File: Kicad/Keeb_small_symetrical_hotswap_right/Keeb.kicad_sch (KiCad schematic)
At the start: 32 parts, among them J2 B2B-XH-A_LF__SN_, J3 MJ-4PP-9_MJ-4PP-9, SW1 CherryMX, SW10 CherryMX, SW11 CherryMX, SW13 CherryMX, SW14 CherryMX, SW15 CherryMX, SW16 CherryMX, SW17 CherryMX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

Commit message: Initial commit
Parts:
- removed SW2: CherryMX, ScottoKeebs_Hotswap:Hotswap_MX_Plated_1.00u, symbol Keeb-rescue:CherryMX-CherryMX
- removed U1: Pico, MCU_RaspberryPi_and_Boards:RPi_Pico_SMD_TH_NO_BACK_HOLES, symbol Keeb-rescue:Pico-MCU_RaspberryPi_and_Boards
- added U3: nice_nano, Nice_nano:nice_nano, symbol nice_nano:nice_nano
- J3: footprint MJ-4PP-9:MJ-4PP-9_no_silk -> MJ-4PP-9:MJ-4PP-9
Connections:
- net 0 is gone; now on net 19: SW20.2
- net 26 is gone; now on net GND: SW3.2
- net 27 is gone; now on net GND: SW4.2
- net 28 is gone; now on net 1: SW5.1
- net 1: now also U3.1 (TX0/P0.06); no longer SW1.1
- net 10: now also J3.3 (C), J3.4 (D), U3.12 (P1.06); no longer SW14.2
- net 11: now also U2.DT, U3.31 (P1.01); no longer SW15.2
- net 12: now also U2.CLK, U3.32 (P1.02); no longer SW17.2
- net 13: now also U3.33 (P1.07)
- net 14: now also SW14.2, U3.13 (NFC1/P0.09); no longer J3.3 (C)
- net 15: now also SW15.2, U3.14 (NFC2/P0.10); no longer J3.1 (A)
- net 16: now also SW17.2, U3.15 (P1.11); no longer SW11.1
- net 17: now also SW18.2, U3.16 (P1.13); no longer SW10.1
- net 18: now also SW19.2, U3.17 (P1.15); no longer SW9.1
- net 19: now also U3.18 (AIN0/P0.02); no longer SW6.1
- net 2: now also SW3.1, U3.2 (RX1/P0.08); no longer U2.SW
- net 20: now also SW16.1, U3.19 (AIN5/P0.29); no longer SW7.1
- net 21: now also SW1.2, U3.20 (AIN7/P0.31); no longer SW8.1
- net 3: now also SW4.1, U3.5 (P0.17); no longer SW19.2
- net 3v3: now also J3.1 (A), U3.21 (VCC), U3.24 (BATIN/P0.04); no longer J3.4 (D)
- net 4: now also SW8.1, U3.6 (P0.20); no longer SW16.1
- net 5: now also SW7.1, U3.7 (P0.22); no longer SW18.2
- net 6: now also SW6.1, U3.8 (P0.24)
- net 7: now also SW11.1, U3.9 (P1.00)
- net 8: now also SW10.1, U3.10 (P0.11); no longer U2.CLK
- net 9: now also SW9.1, U3.11 (P1.04); no longer U2.DT
- net GND: now also SW1.1, U3.23 (GND), U3.3 (GND), U3.4 (GND); no longer SW1.2, SW3.1, SW4.1
- new net RST: U3.22 (RST)

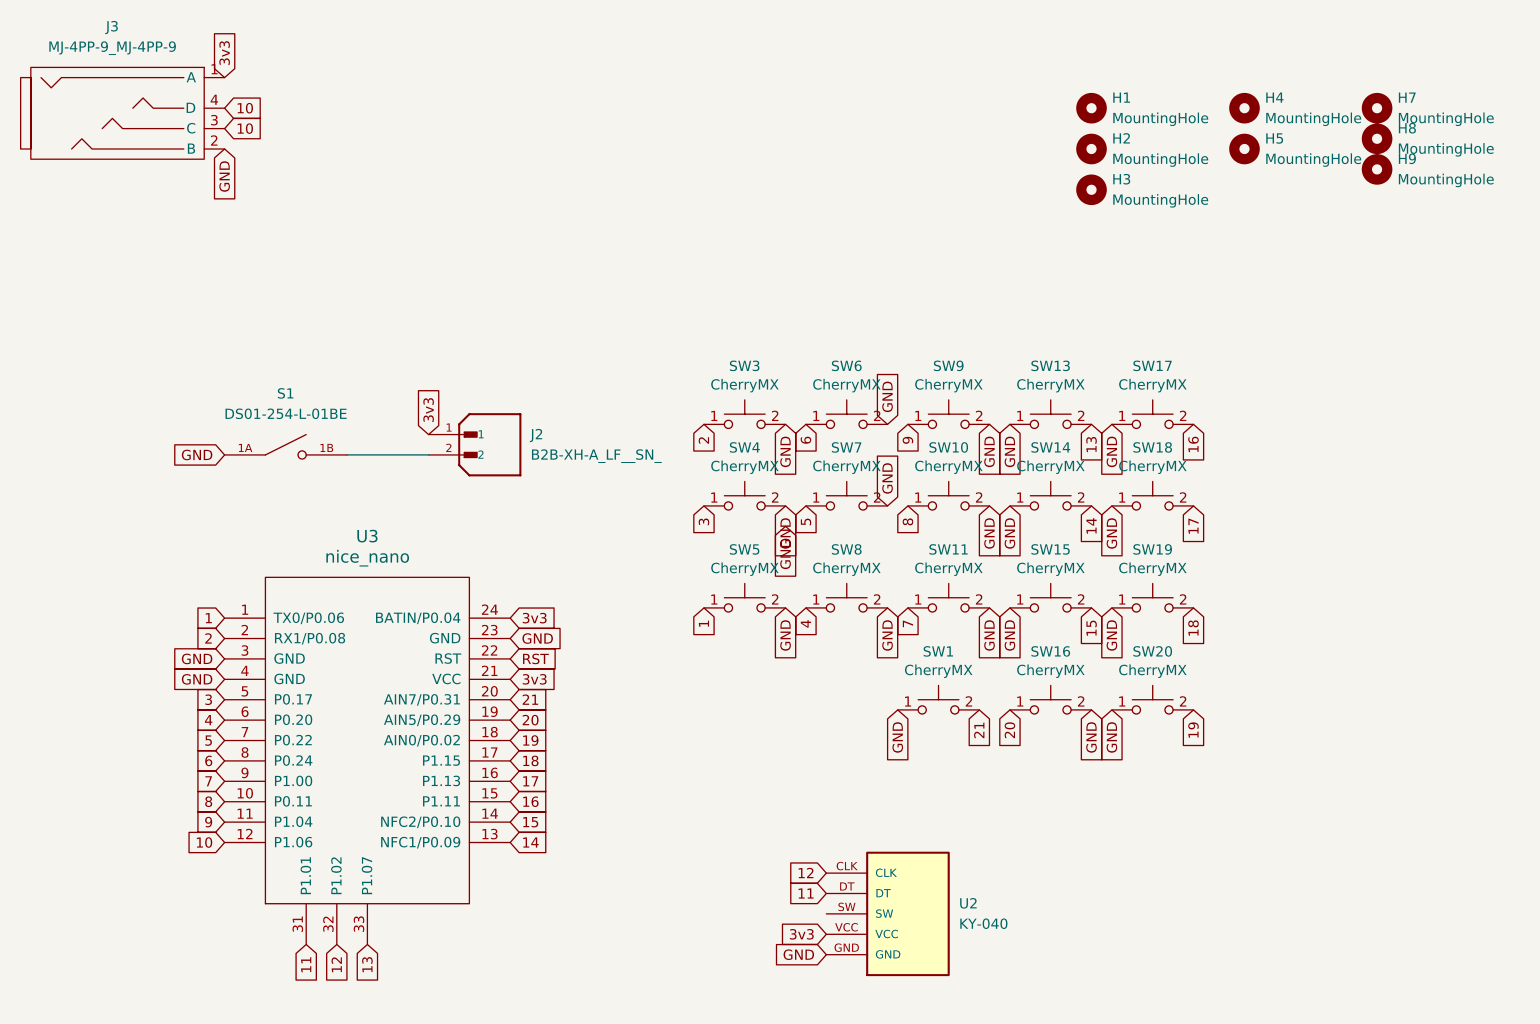
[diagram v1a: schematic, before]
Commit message: current version, all problems fixed, software compiled for CP 9.0
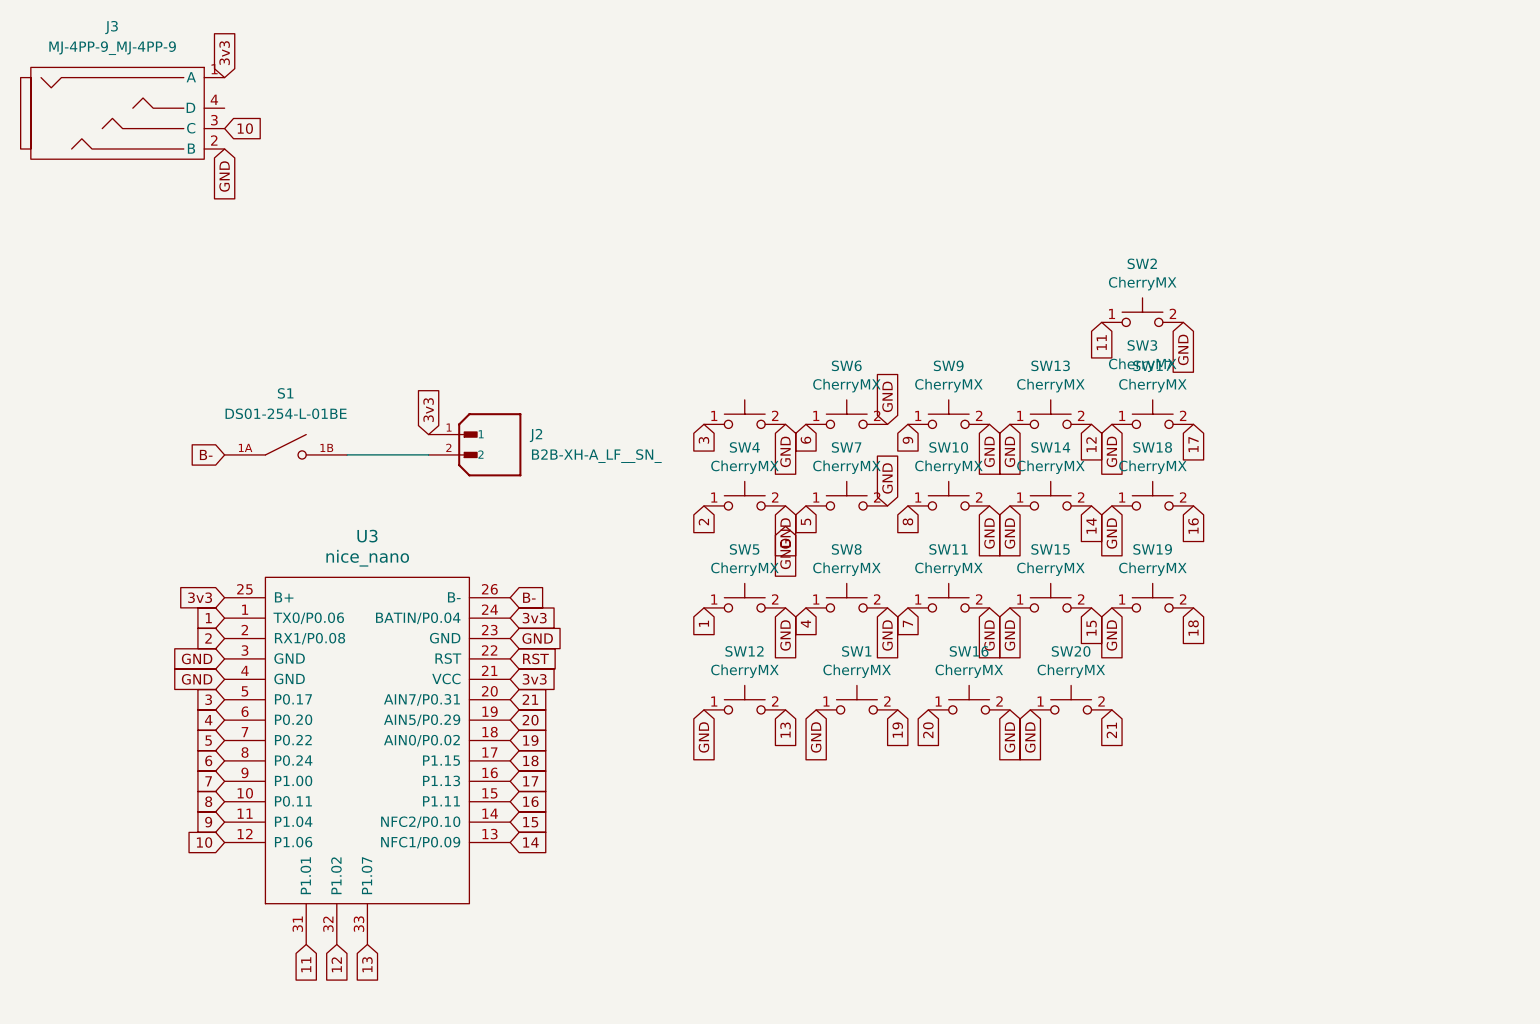
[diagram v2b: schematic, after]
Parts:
- removed H1, H2, H3, H4, H5, H7, H8, H9: MountingHole, MountingHole:MountingHole_3.2mm_M3, symbol Mechanical:MountingHole
- removed U2: KY-040, KY-040:KY-040-PORT, symbol KY-040:KY-040
- added SW12, SW2: CherryMX, ScottoKeebs_Hotswap:Hotswap_Choc_V1_Plated_1.00u, symbol Keeb-rescue:CherryMX-CherryMX
- SW1, SW10, SW11, SW13, SW14, SW15, SW16, SW17, SW18, SW19, SW20, SW3, SW4, SW5, SW6, SW7, SW8, SW9: footprint ScottoKeebs_Hotswap:Hotswap_MX_Plated_1.00u -> ScottoKeebs_Hotswap:Hotswap_Choc_V1_Plated_1.00u
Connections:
- net 10: no longer J3.4 (D)
- net 11: now also SW2.1
- net 12: now also SW13.2
- net 13: now also SW12.2; no longer SW13.2
- net 16: now also SW18.2; no longer SW17.2
- net 17: now also SW17.2; no longer SW18.2
- net 19: now also SW1.2; no longer SW20.2
- net 2: now also SW4.1; no longer SW3.1
- net 21: now also SW20.2; no longer SW1.2
- net 3: now also SW3.1; no longer SW4.1
- net 3v3: now also U3.25 (B+)
- net GND: now also SW12.1, SW2.2; no longer S1.1A
- new net B-: S1.1A, U3.26 (B-)
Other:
- moved on the sheet: SW1, SW16, SW20
